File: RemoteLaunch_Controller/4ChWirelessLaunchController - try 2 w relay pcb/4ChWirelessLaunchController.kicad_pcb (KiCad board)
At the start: 2 copper layers, 75.2 x 99.7 mm, 23 parts, among them J1 Pad power and switch, J2 Control board, J3 Pad ch 1, J4 Pad ch 2, J5 Pad ch 3, J6 Pad ch 4, J7 Armed siren, J8 LED/Buzzer Continuity indicat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, J9 LED power indicator, K1 G8N-1U-DC12, K2 Ch 1 relay, K3 G8N-1U-DC12, K4 G8N-1U-DC12, K5 G8N-1U-DC12

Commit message: Adding 4ch relay board
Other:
- net class Default removed

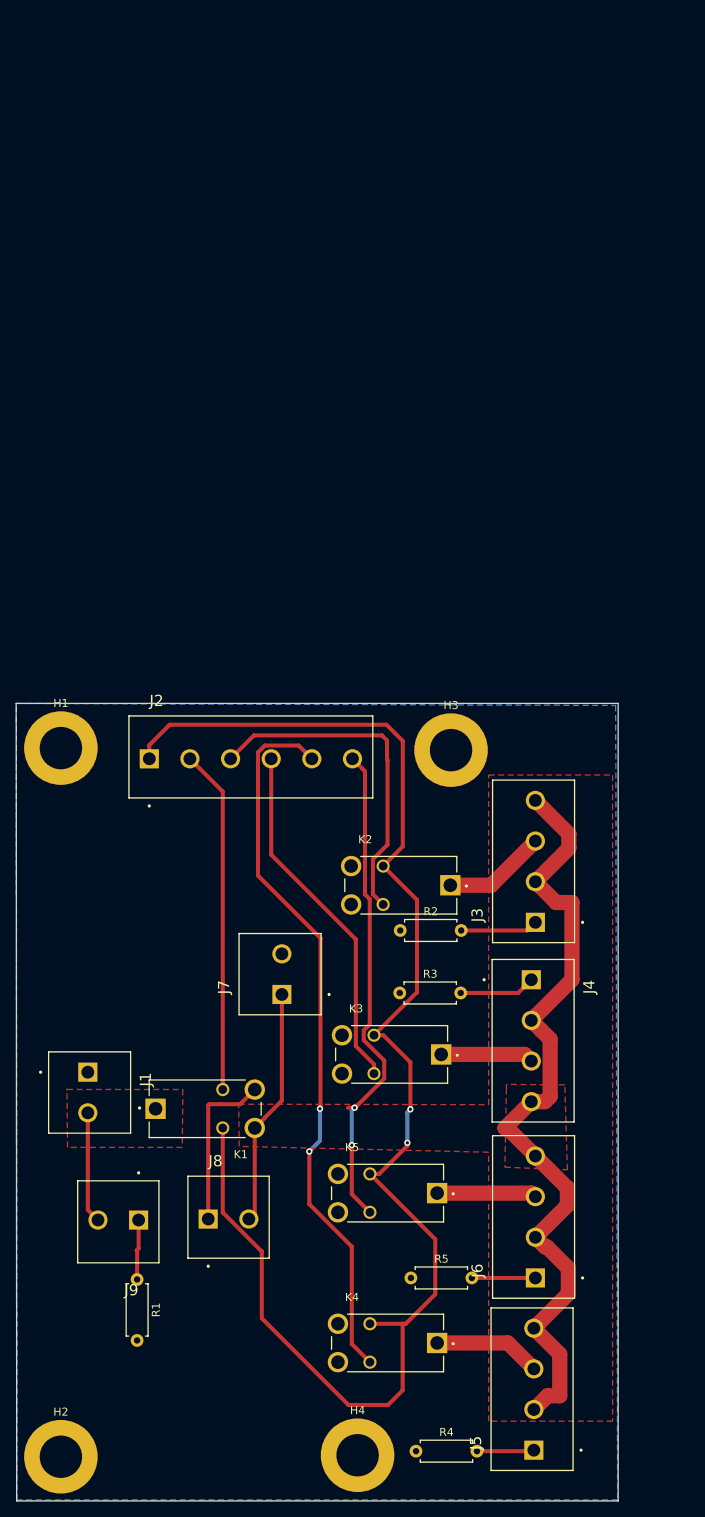
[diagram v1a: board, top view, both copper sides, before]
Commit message: Fixing glitch in relay board;  Sending REv4_3 to fab
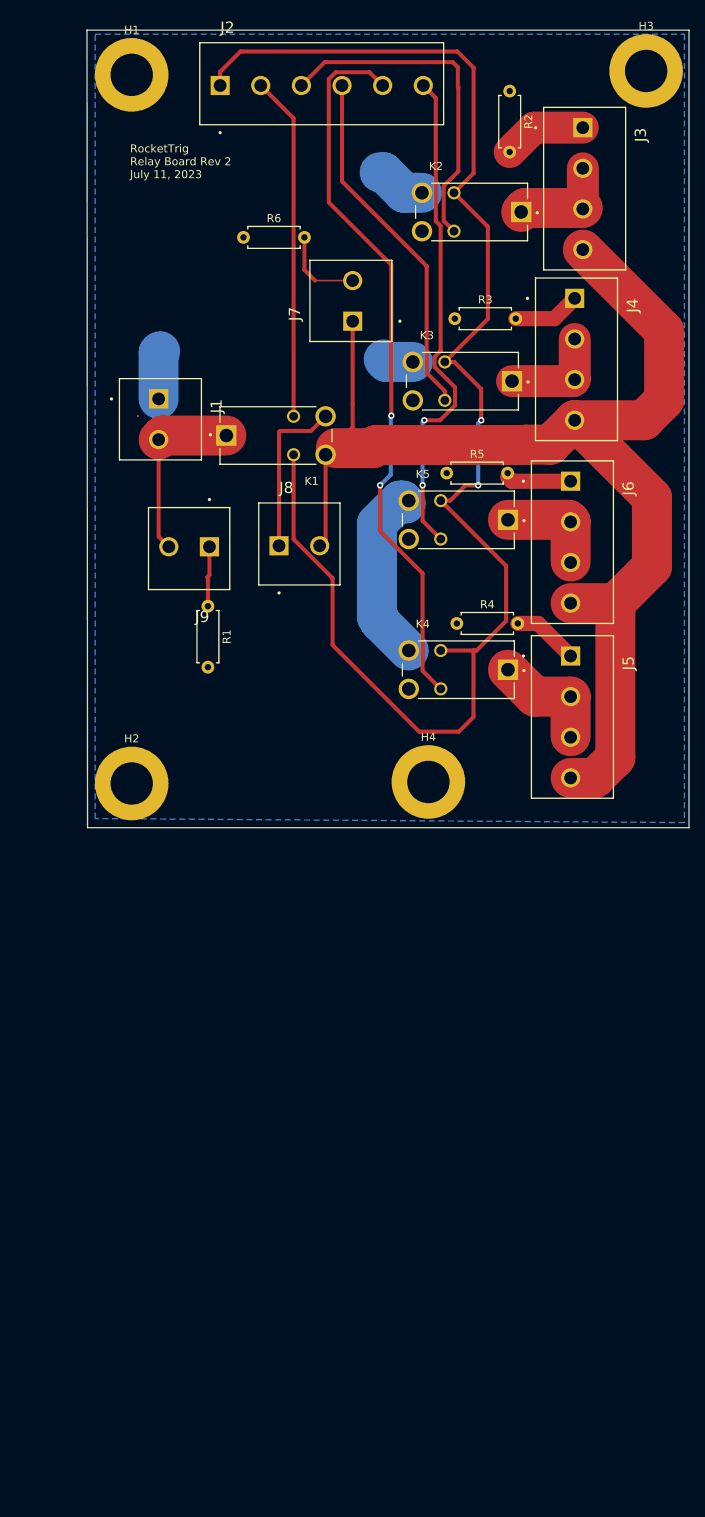
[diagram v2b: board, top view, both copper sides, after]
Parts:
- added R6: R, Resistor_THT:R_Axial_DIN0207_L6.3mm_D2.5mm_P7.62mm_Horizontal, F.Cu at (92.9, 68.2)
- moved R2 105.8 mm to (126.2, 50.0), turned to -90 degrees
- moved R4 103.6 mm to (119.6, 116.5)
- moved R5 100.7 mm to (118.3, 97.7)
- moved J6 99.7 mm to (133.8, 98.7), turned to -90 degrees
- moved J3 99.5 mm to (135.3, 54.5), turned to -90 degrees
- moved J5 99.4 mm to (133.8, 120.6), turned to -90 degrees
- moved H3 88.3 mm to (143.3, 47.4)
- moved J4 85.3 mm to (134.3, 75.9)
- moved H1 84.6 mm to (79.0, 47.9)
- moved H4 84.6 mm to (116.0, 136.3)
- moved J8 84.6 mm to (97.4, 106.8)
- moved K4 84.6 mm to (119.8, 122.3)
- moved R1 84.6 mm to (88.5, 114.3)
- moved J2 84.6 mm to (90.0, 49.3)
- moved J7 84.6 mm to (106.6, 78.7)
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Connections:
- J1 pad 1: Net-(J1-Pad1) -> Net-(J1-Pin_1)
- J3 pad 2: Pad_common -> Net-(J3-Pin_2)
- J3 pad 3: Net-(J3-Pad3) -> Net-(J3-Pin_2)
- J4 pad 2: Pad_common -> Net-(J4-Pin_2)
- J4 pad 3: Net-(J4-Pad3) -> Net-(J4-Pin_2)
- J5 pad 2: Pad_common -> Net-(J5-Pin_2)
- J5 pad 3: Net-(J5-Pad3) -> Net-(J5-Pin_2)
- J6 pad 2: Pad_common -> Net-(J6-Pin_2)
- J6 pad 3: Net-(J6-Pad3) -> Net-(J6-Pin_2)
- J7 pad 2: Net-(J1-Pad1) -> Net-(J7-Pin_2)
- K2 pad 1: Net-(J3-Pad3) -> Net-(J3-Pin_2)
- K2 pad 3: Net-(J1-Pad1) -> Net-(J1-Pin_1)
- K2 pad 4: Net-(K2-Pad4) -> unconnected-(K2-Pad4)
- K3 pad 1: Net-(J4-Pad3) -> Net-(J4-Pin_2)
- K3 pad 3: Net-(J1-Pad1) -> Net-(J1-Pin_1)
- K3 pad 4: Net-(K3-Pad4) -> unconnected-(K3-Pad4)
- K4 pad 1: Net-(J5-Pad3) -> Net-(J5-Pin_2)
- K4 pad 3: Net-(J1-Pad1) -> Net-(J1-Pin_1)
- K4 pad 4: Net-(K4-Pad4) -> unconnected-(K4-Pad4)
- K5 pad 1: Net-(J6-Pad3) -> Net-(J6-Pin_2)
- K5 pad 3: Net-(J1-Pad1) -> Net-(J1-Pin_1)
- K5 pad 4: Net-(K5-Pad4) -> unconnected-(K5-Pad4)
- R1 pad 2: Net-(J1-Pad1) -> Net-(J1-Pin_1)
- R2 pad 1: Net-(J1-Pad1) -> Net-(J1-Pin_1)
- R3 pad 1: Net-(J1-Pad1) -> Net-(J1-Pin_1)
- R4 pad 1: Net-(J1-Pad1) -> Net-(J1-Pin_1)
- R5 pad 1: Net-(J1-Pad1) -> Net-(J1-Pin_1)
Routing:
- net Net-(J1-Pin_1): track 0.00 -> 38.6 mm
- net Pad_common: track 131.1 -> 156.6 mm
- net Net-(J5-Pin_2): track 0.00 -> 14.2 mm
- net Net-(J5-Pad3): track 13.4 -> 0.00 mm
- net Net-(J4-Pin_2): track 0.00 -> 13.0 mm
- net Net-(J3-Pad3): track 12.9 -> 0.00 mm
- net Net-(J6-Pin_2): track 0.00 -> 12.9 mm
- net Net-(J3-Pin_2): track 0.00 -> 12.9 mm
- net Net-(J6-Pad3): track 12.5 -> 0.00 mm
- net Net-(J4-Pad3): track 11.6 -> 0.00 mm
- net Net-(J7-Pin_2): track 0.00 -> 11.1 mm
- net Net-(J1-Pin_2): track 13.9 -> 22.6 mm
- net Net-(J5-Pin_1): track 7.16 -> 8.29 mm
- net Net-(J4-Pin_1): track 9.51 -> 8.42 mm
- net Relay_common: track 184.9 -> 185.8 mm
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- added copper zone on B.Cu, net Net-(J1-Pin_1)
- removed copper zone on B.Cu, net Net-(J1-Pad1)
- removed copper zone on F.Cu, net Pad_common
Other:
- board text added: "RocketTrig Relay Board Rev 2 July 11, 2023"

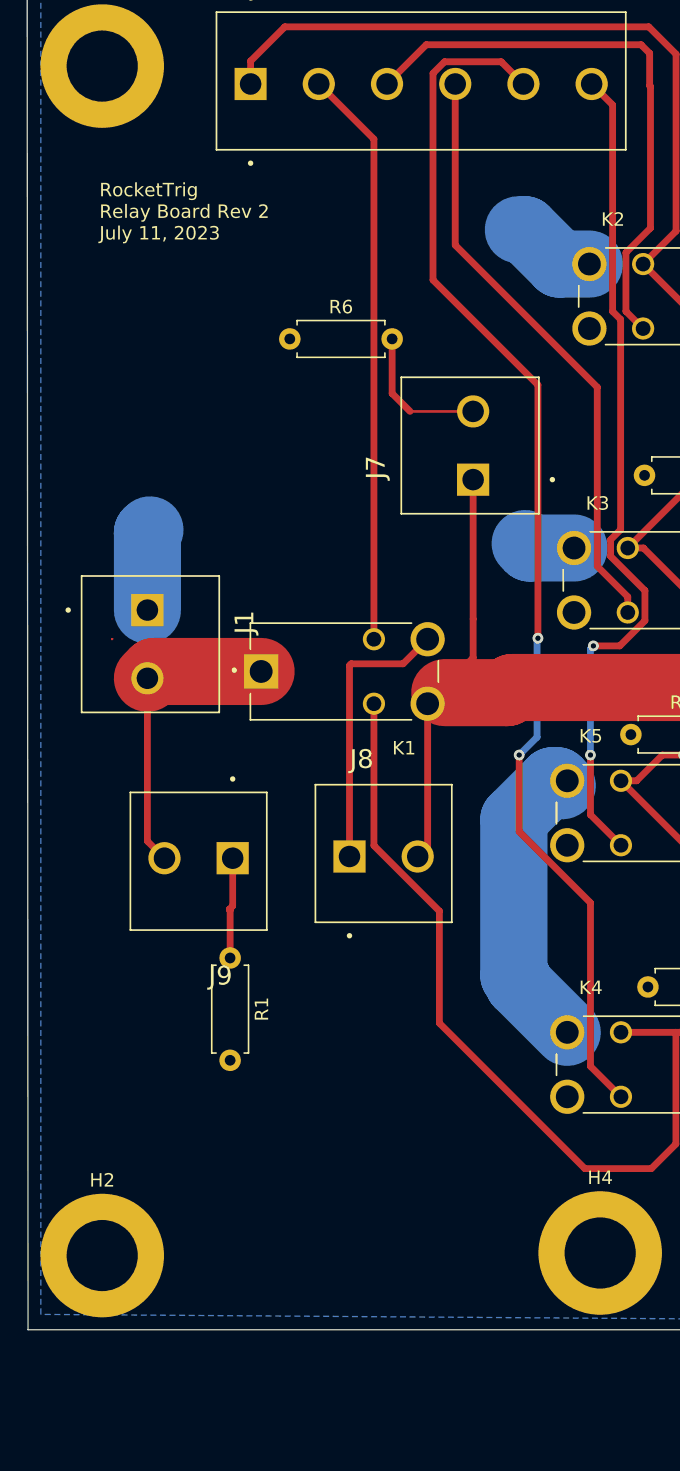
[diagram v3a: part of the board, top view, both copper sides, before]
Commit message: Working on adding polling / heartbeat;  Seem to have broken launch
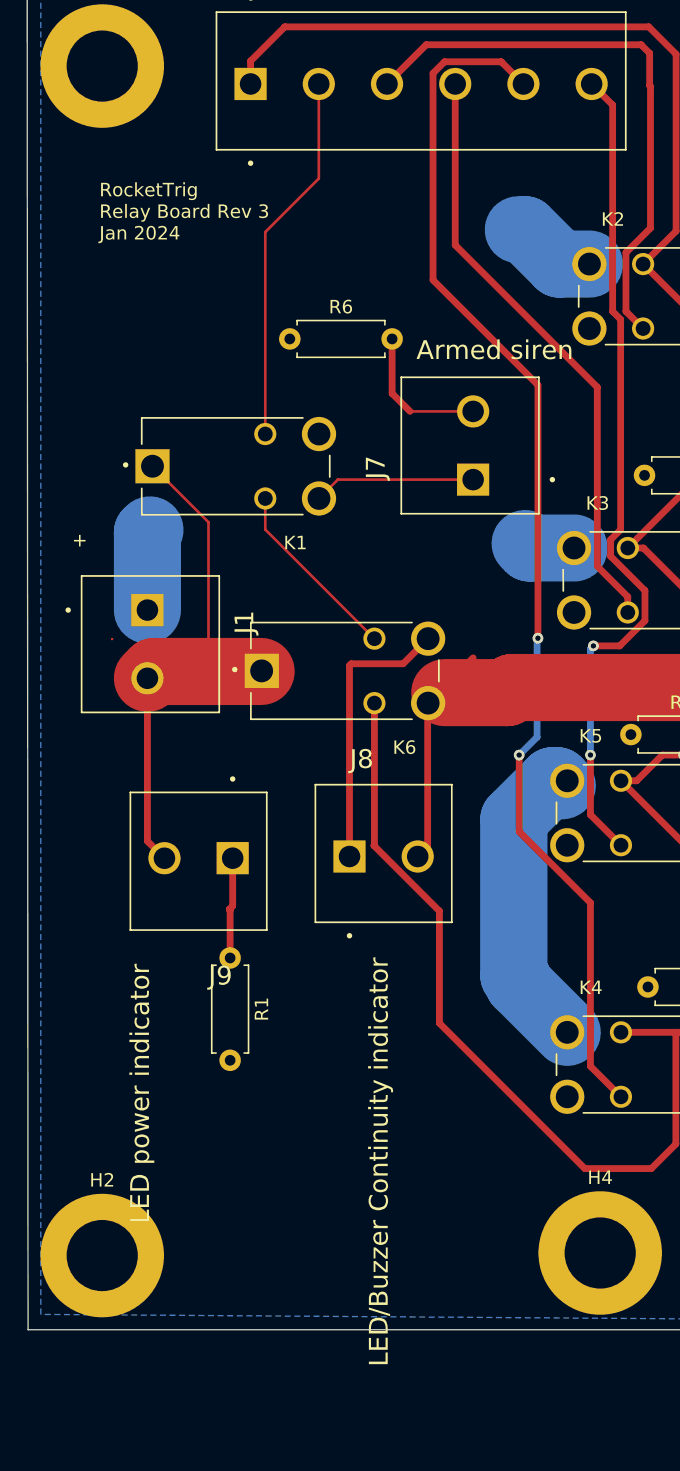
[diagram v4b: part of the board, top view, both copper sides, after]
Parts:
- added K6: G8N-1L-DC12, RocketTrig_Library:RELAY_G8N-1U-DC12, F.Cu at (97.0, 93.0)
- K1: value G8N-1U-DC12 -> G8N-1L-DC12; footprint CameraTriggerPCB:RELAY_G8N-1U-DC12 -> RocketTrig_Library:RELAY_G8N-1U-DC12
- moved K1 17.3 mm to (88.9, 77.7)
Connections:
- J7 pad 1: Pad_common -> Net-(J7-Pin_1)
- K1 pad 2: Relay_common -> Net-(K1-Pad2)
- K1 pad 3: Pad_common -> Net-(J7-Pin_1)
- K1 pad 4: Net-(J8-Pin_1) -> unconnected-(K1-Pad4)
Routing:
- net Net-(J1-Pin_2): track 22.6 -> 39.6 mm
- net ArmedRelayPin1: track 43.1 -> 27.7 mm
- net Net-(K1-Pad2): track 0.00 -> 13.8 mm
- net Pad_common: track 156.6 -> 143.3 mm
- net Net-(J7-Pin_1): track 0.00 -> 12.1 mm
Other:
- board text added: "+"
- board text added: "RocketTrig Relay Board Rev 3 Jan 2024"
- board text removed: "RocketTrig Relay Board Rev 2 July 11, 2023"
